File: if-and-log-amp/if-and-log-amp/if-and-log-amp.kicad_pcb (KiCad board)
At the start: 2 copper layers, 92.2 x 52.3 mm, 58 parts, among them J301 Conn_Coaxial, J302 Conn_01x01_Male, J303 Conn_01x01_Male, J304 Conn_01x01_Male, J305 Conn_01x01_Male, J306 Conn_01x01_Male, U301 AD603AQ, U302 L78L05_TO92, U303 LM317L_TO92, U304 AD8307AN, U305 CA3140

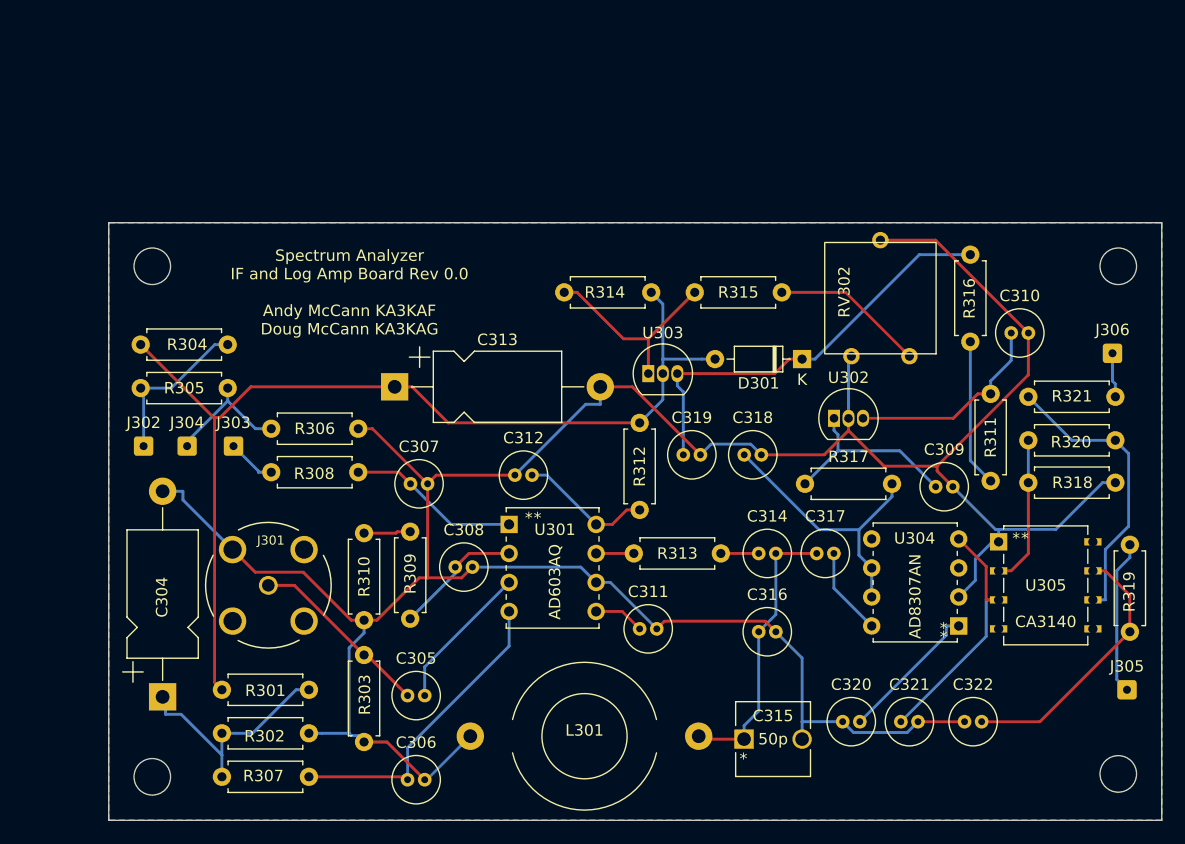
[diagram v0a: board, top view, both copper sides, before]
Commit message: Improvements to if and log amp
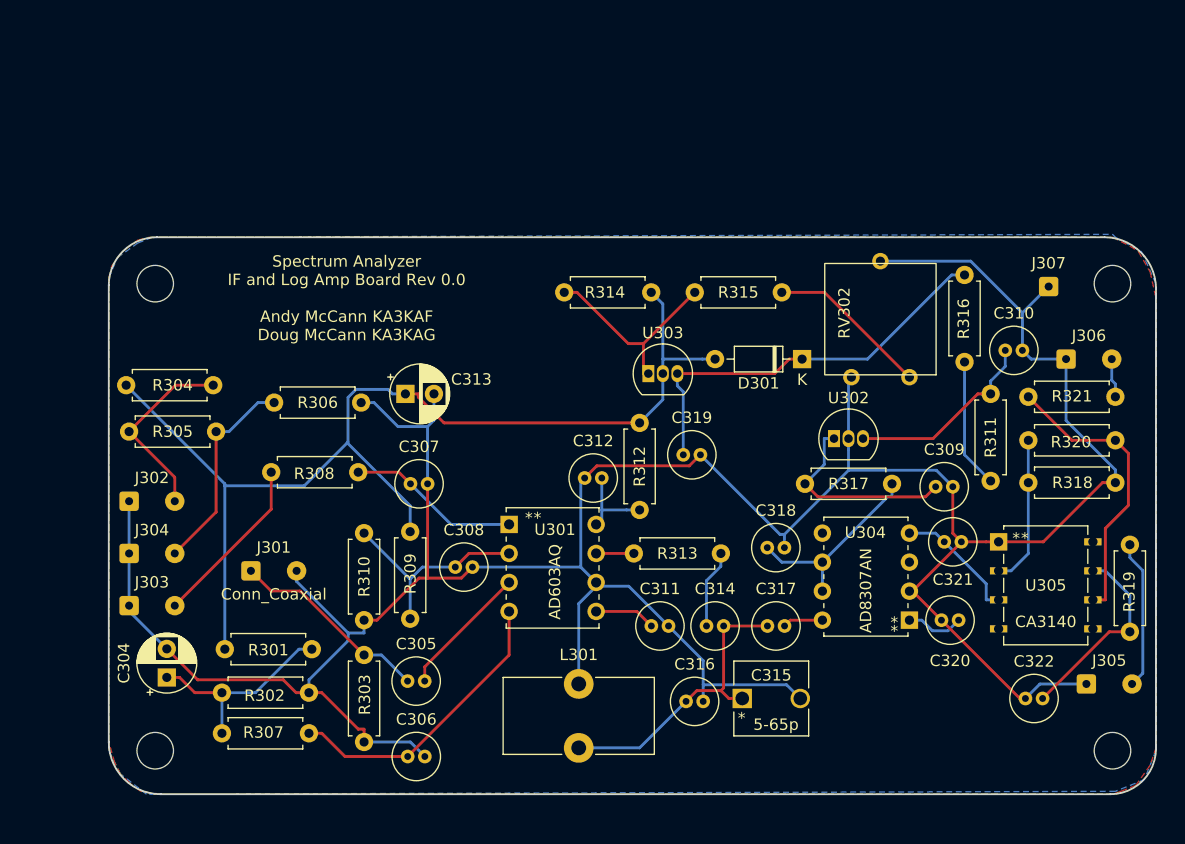
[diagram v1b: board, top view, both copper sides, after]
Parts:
- added J307: Board to Box Ground, Connector_Wire:SolderWire-0.15sqmm_1x01_D0.5mm_OD1.5mm, F.Cu at (177.6, 84.7)
- C304, C313: footprint Capacitor_THT:CP_Axial_L11.0mm_D6.0mm_P18.00mm_Horizontal -> Capacitor_THT:CP_Radial_D5.0mm_P2.50mm
- C305: value .1u -> .01u
- C315: value 50p -> 5-65p
- J301: footprint if-log-amp:TE_5-1634503-1 -> Connector_Wire:SolderWire-0.15sqmm_1x02_P4mm_D0.5mm_OD1.5mm
- J302, J303, J304, J305, J306: value Conn_01x01_Male -> Conn_01x02_Male; footprint Connector_Wire:SolderWire-0.15sqmm_1x01_D0.5mm_OD1.5mm -> Connector_Wire:SolderWire-0.15sqmm_1x02_P4mm_D0.5mm_OD1.5mm
- L301: footprint Inductor_THT:L_Toroid_Horizontal_D12.7mm_P20.00mm_Diameter14-5mm_Amidon-T50 -> Inductor_THT:L_Toroid_Vertical_L13.0mm_W6.5mm_P5.60mm
- moved J303 16.7 mm to (97.1, 112.7)
- moved C321 16.2 mm to (168.5, 107.1)
- moved C320 12.4 mm to (168.3, 113.9)
- moved J304 10.7 mm to (97.1, 108.1)
- moved L301 10.5 mm to (136.5, 119.5)
- moved C316 8.81 mm to (145.9, 121.1)
- moved C318 8.38 mm to (153.0, 107.6)
- moved C314 7.82 mm to (147.7, 114.5)
- moved C317 7.68 mm to (153.0, 114.5)
- moved C312 6.11 mm to (137.0, 101.5)
- moved C322 5.71 mm to (175.6, 120.8)
- moved J302 4.99 mm to (97.1, 103.5)
- moved U304 4.35 mm to (165.5, 113.9)
- moved J306 4.10 mm to (179.2, 91.1)
- moved R305 3.94 mm to (97.1, 97.4)
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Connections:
- J302 pad 1: Net-(C301-Pad3) -> GND
- J303 pad 1: Net-(C302-Pad3) -> GND
- J304 pad 1: Net-(C303-Pad3) -> GND
- J305 pad 1: Net-(C324-Pad1) -> GND
- J306 pad 1: Net-(C323-Pad1) -> GND
- R309 pad 2: V+10 -> +10
- R310 pad 1: V+10 -> Net-(C308-Pad1)
- R319 pad 2: Net-(C324-Pad1) -> Net-(J305-Pad2)
- R321 pad 2: Net-(C323-Pad1) -> Net-(R321-Pad2)
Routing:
- net GND: track 253.3 -> 278.5 mm
- net Net-(C324-Pad1): track 13.5 -> 0.00 mm
- net Net-(J305-Pad2): track 0.00 -> 13.1 mm
- net Net-(C321-Pad1): track 22.3 -> 11.1 mm
- net Net-(C302-Pad3): track 4.31 -> 15.2 mm
- net Net-(C320-Pad2): track 12.6 -> 5.07 mm
- net Net-(C308-Pad1): track 11.4 -> 18.8 mm
- net +10: track 90.1 -> 97.5 mm
- net Net-(C303-Pad3): track 11.4 -> 18.3 mm
- net Net-(C318-Pad1): track 24.3 -> 17.5 mm
- net Net-(C322-Pad2): track 23.6 -> 17.4 mm
- net Net-(C317-Pad2): track 7.72 -> 3.52 mm
- net Net-(C312-Pad2): track 11.7 -> 7.58 mm
- net V+10: track 4.09 -> 0.00 mm
- net Net-(C323-Pad1): track 3.92 -> 0.00 mm
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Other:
- board size 92.2 x 52.3 mm -> 91.7 x 48.8 mm

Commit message: updates to 15v supply and if and log amp boards so boards can be sent to fab
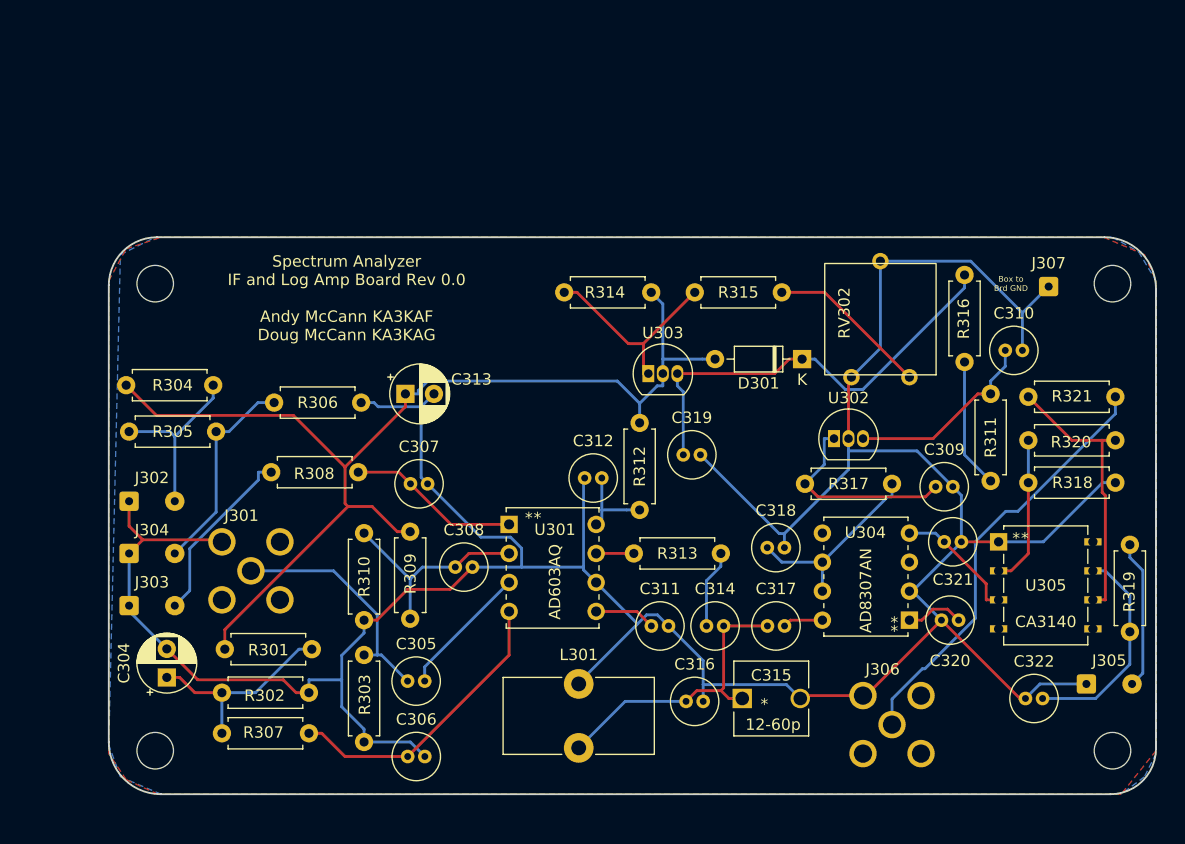
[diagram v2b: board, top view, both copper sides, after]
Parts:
- C315: value 5-65p -> 12-60p
- C316: value 220p -> 180p
- J301: footprint Connector_Wire:SolderWire-0.15sqmm_1x02_P4mm_D0.5mm_OD1.5mm -> if-log-amp:MOLEX_73391-0060
- J306: value Conn_01x02_Male -> Conn_Coaxial; footprint Connector_Wire:SolderWire-0.15sqmm_1x02_P4mm_D0.5mm_OD1.5mm -> if-log-amp:MOLEX_73391-0060
- moved J306 35.4 mm to (163.9, 123.1)
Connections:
- J306 pad 1: GND -> Net-(C323-Pad1)
- J306 pad 2: Net-(R321-Pad2) -> GND
- R321 pad 2: Net-(R321-Pad2) -> Net-(C323-Pad1)
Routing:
- net Net-(C323-Pad1): track 0.00 -> 37.6 mm
- net Net-(R321-Pad2): track 3.43 -> 0.00 mm
- net Net-(C305-Pad1): track 17.7 -> 20.9 mm
- net Net-(C319-Pad1): track 36.1 -> 38.9 mm
- net GND: track 278.5 -> 280.3 mm
- net Net-(C322-Pad2): track 17.4 -> 19.0 mm
- net Net-(R320-Pad1): track 25.6 -> 24.4 mm
- net Net-(C301-Pad3): track 16.8 -> 15.7 mm
- net Net-(C302-Pad3): track 15.2 -> 15.8 mm
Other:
- board text added: "Box to Brd GND"

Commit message: Rev 1 Changes for if and log amp
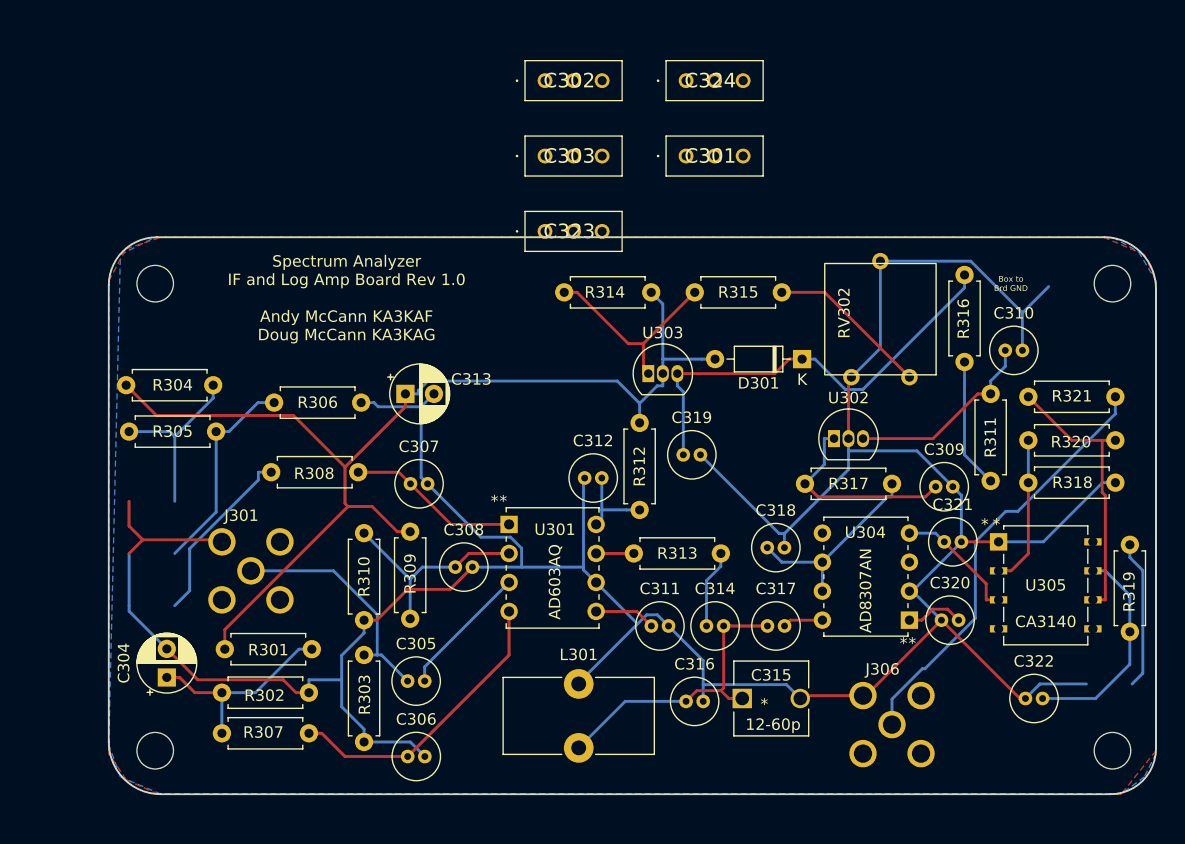
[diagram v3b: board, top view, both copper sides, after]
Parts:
- removed J302, J303, J304, J305: Conn_01x02_Male, Connector_Wire:SolderWire-0.15sqmm_1x02_P4mm_D0.5mm_OD1.5mm
- removed J307: Board to Box Ground, Connector_Wire:SolderWire-0.15sqmm_1x01_D0.5mm_OD1.5mm
- added C301: 5n, if-log-amp:DSS1NB32A102Q91A, F.Cu at (145.9, 73.3)
- added C302: 5n, if-log-amp:DSS1NB32A102Q91A, F.Cu at (133.5, 66.7)
- added C303: 5n, if-log-amp:DSS1NB32A102Q91A, F.Cu at (133.5, 73.3)
- added C323: 1n, if-log-amp:DSS1NB32A102Q91A, F.Cu at (133.5, 79.9)
- added C324: 1n, if-log-amp:DSS1NB32A102Q91A, F.Cu at (145.9, 66.7)
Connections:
- R319 pad 2: Net-(C324-Pad1) -> +15
- U305 pad 1: GND -> unconnected-(U305-Pad1)
- U305 pad 4: unconnected-(U305-Pad4) -> GND
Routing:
- net Net-(C324-Pad1): track 13.1 -> 0.00 mm
- net +15: track 11.4 -> 24.4 mm
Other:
- board text added: "Spectrum Analyzer IF and Log Amp Board Rev 1.0 Andy McCann KA3KAF Doug McCann KA3KAG"
- board text removed: "Spectrum Analyzer IF and Log Amp Board Rev 0.0 Andy McCann KA3KAF Doug McCann KA3KAG"

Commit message: minor changes to log amp board
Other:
- board text added: "10V Adj"
- board text added: "Filter adjust"
- board text added: "Front Panel IF Gain"
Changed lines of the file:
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@@
     (effects (font (size 1 1) (thickness 0.15)))
+  )
+  (gr_text "Filter adjust" (at 150.7236 127.4064) (layer "F.SilkS")
+    (effects (font (size 1.5 1.5) (thickness 0.3)))
+  )
+  (gr_text "10V Adj" (at 162.9156 84.2264) (layer "F.SilkS")
+    (effects (font (size 1.5 1.5) (thickness 0.3)))
   )
   (gr_text "Box to \nBrd GND" (at 174.3456 84.4804) (layer "F.SilkS")
     (effects (font (size 0.5 0.5) (thickness 0.1)))
   )
+  (gr_text "Front Panel IF Gain" (at 101.7016 104.8004) (layer "F.SilkS")
+    (effects (font (size 1.5 1.5) (thickness 0.3)))
+  )
   (segment (start 102.8918 120.2944) (end 101.5569 118.9595) (width 0.25) (layer "F.Cu") (net 1))

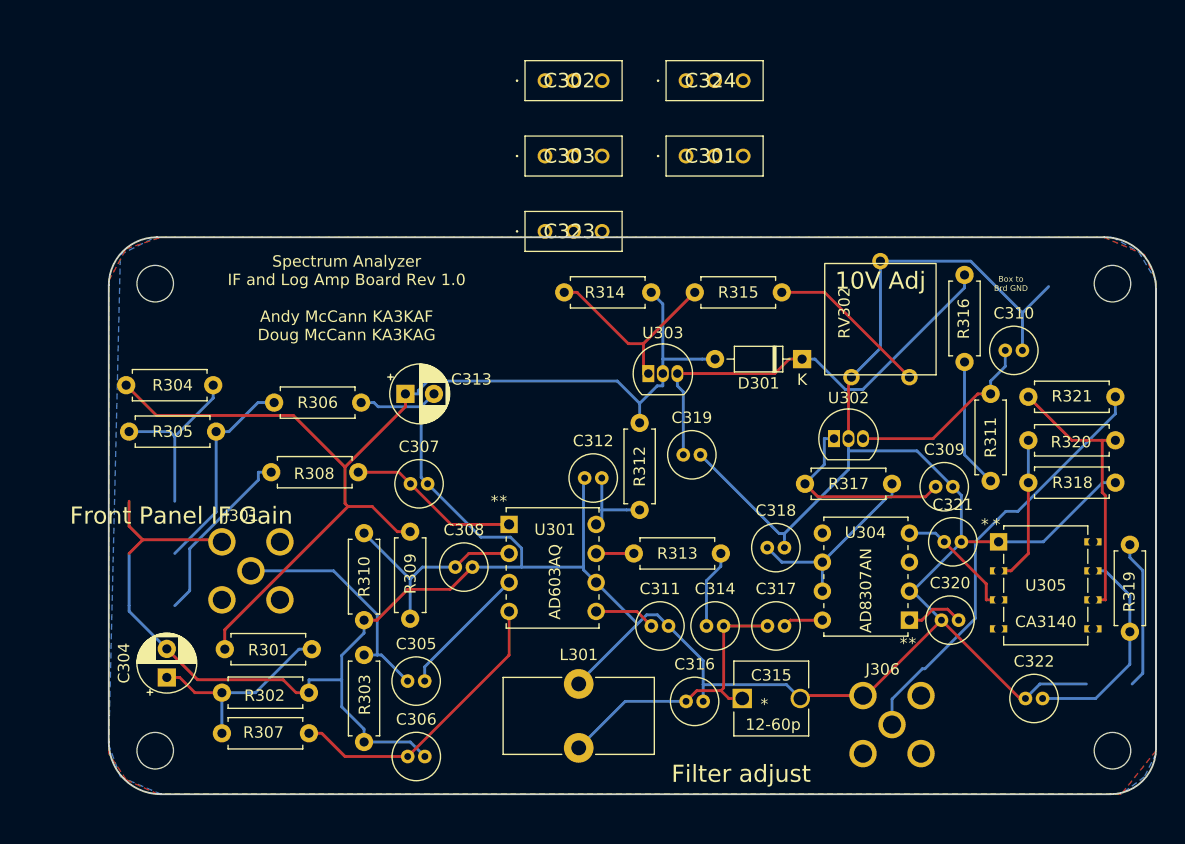
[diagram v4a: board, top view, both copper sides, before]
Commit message: further improvements to if-log amp
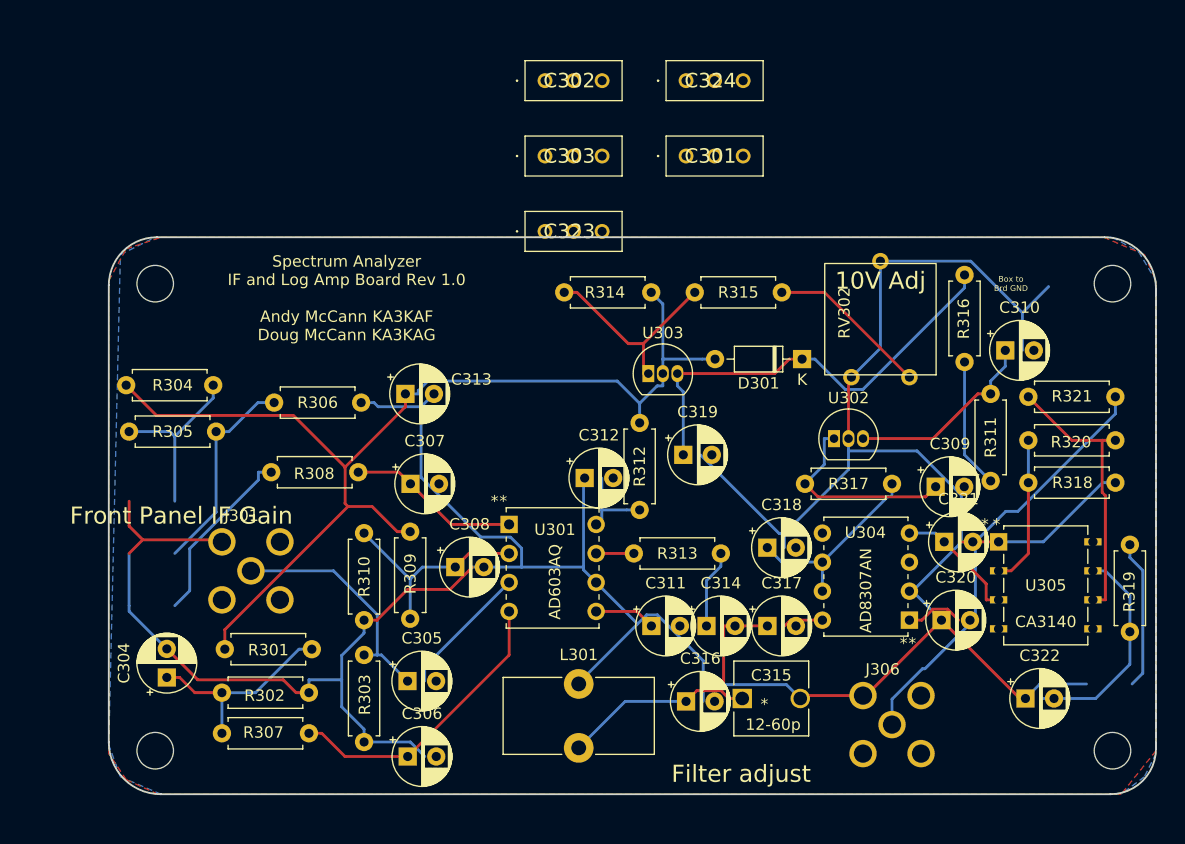
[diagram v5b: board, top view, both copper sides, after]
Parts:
- C305, C306, C307, C308, C309, C310, C312, C314, C316, C317, C318, C319, C320, C321, C322: footprint Capacitor_THT:C_Radial_D4.0mm_H5.0mm_P1.50mm -> Capacitor_THT:CP_Radial_D5.0mm_P2.50mm
- C311: value 18u -> 18p; footprint Capacitor_THT:C_Radial_D4.0mm_H5.0mm_P1.50mm -> Capacitor_THT:CP_Radial_D5.0mm_P2.50mm
- D301: value 1N4152 -> 1N4150
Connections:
- J306 pad 1: Net-(C323-Pad1) -> /Out
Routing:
- net GND: track 280.3 -> 401.8 mm
- net Net-(C323-Pad1): track 37.6 -> 0.00 mm
- net Net-(C306-Pad1): track 25.9 -> 0.00 mm
- net Net-(C308-Pad1): track 18.8 -> 0.00 mm
- net +5: track 17.8 -> 0.00 mm
- net Net-(C321-Pad1): track 11.1 -> 0.00 mm
- net Net-(C311-Pad1): track 5.36 -> 0.00 mm
- net Net-(C320-Pad2): track 5.10 -> 0.00 mm
